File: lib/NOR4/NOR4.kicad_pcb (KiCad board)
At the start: 2 copper layers, 8 parts

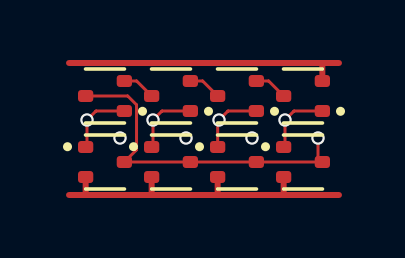
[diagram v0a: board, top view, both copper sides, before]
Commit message: All cells now use 1mm*4mm grid rather than 1.1mm*4.4mm
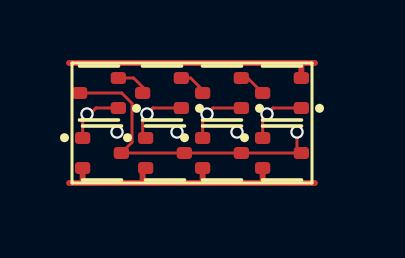
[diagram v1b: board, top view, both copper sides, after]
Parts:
- moved N4 0.76 mm to (7.00, 3.00)
- moved P4 0.71 mm to (7.00, 1.00)
- moved N3 0.58 mm to (5.00, 3.00)
- moved P3 0.51 mm to (5.00, 1.00)
- moved N2 0.36 mm to (3.10, 3.00)
- moved N1 0.32 mm to (1.00, 3.00)
- moved P2 0.32 mm to (3.00, 1.00)
- moved P1 0.22 mm to (0.90, 1.00)
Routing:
- net GND: track 11.4 -> 10.3 mm
- net Y: track 11.6 -> 10.5 mm
- net VDD: track 9.63 -> 8.73 mm

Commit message: Make the pads of my SOT523 footprint very slightly smaller, which is enough to route all the cells and leave the mosfets exactly on the grid
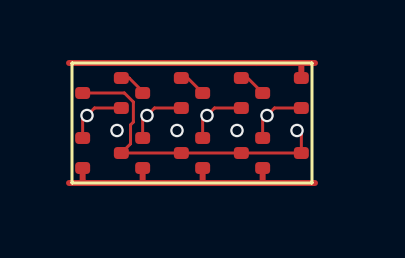
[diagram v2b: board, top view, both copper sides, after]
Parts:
- N1, N2, N3, N4, P1, P2, P3, P4: footprint Package_TO_SOT_SMD:SOT-523 -> RV523:SOT523
- moved N2 0.10 mm to (3.00, 3.00)
- moved P1 0.10 mm to (1.00, 1.00)

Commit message: Propagate MOSFET values to the cells' PCBs
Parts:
- N1, N2, N3, N4: value (none) -> NMOS
- P1, P2, P3, P4: value (none) -> PMOS
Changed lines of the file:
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@@
 			)
 		)
-		(property "Value" ""
+		(property "Value" "PMOS"
 			(at 0 0 180)
 			(layer "F.Fab")
@@
 			)
 		)
-		(property "Value" ""
+		(property "Value" "PMOS"
 			(at 0 0 180)
 			(layer "F.Fab")
@@
 			)
 		)
-		(property "Value" ""
+		(property "Value" "NMOS"
 			(at 0 0 0)
 			(layer "F.Fab")
@@
 			)
 		)
-		(property "Value" ""
+		(property "Value" "PMOS"
 			(at 0 0 180)
 			(layer "F.Fab")
@@
 			)
 		)
-		(property "Value" ""
+		(property "Value" "PMOS"
 			(at 0 0 180)
 			(layer "F.Fab")
@@
 			)
 		)
-		(property "Value" ""
+		(property "Value" "NMOS"
 			(at 0 0 0)
 			(layer "F.Fab")
@@
 			)
 		)
-		(property "Value" ""
+		(property "Value" "NMOS"
 			(at 0 0 0)
 			(layer "F.Fab")
@@
 			)
 		)
-		(property "Value" ""
-			(at 0 0 0)
-			(layer "F.Fab")
+		(property "Value" "NMOS"
+			(at 0 0 0)
+			(layer "F.Fab")
